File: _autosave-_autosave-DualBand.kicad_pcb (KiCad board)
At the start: 2 copper layers, 99.6 x 50.2 mm, 66 parts, among them J1 Conn_01x03_Male, J2 Conn_01x03_Male, J3 Conn_01x10_Male, J4 Conn_01x03_Male, J5 Conn_01x02_Male, J6 Conn_01x10_Male, J7 Conn_01x01_Male, P1 AD8402ARUZ1, SW1 SW_Push, U1 LD1117V33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

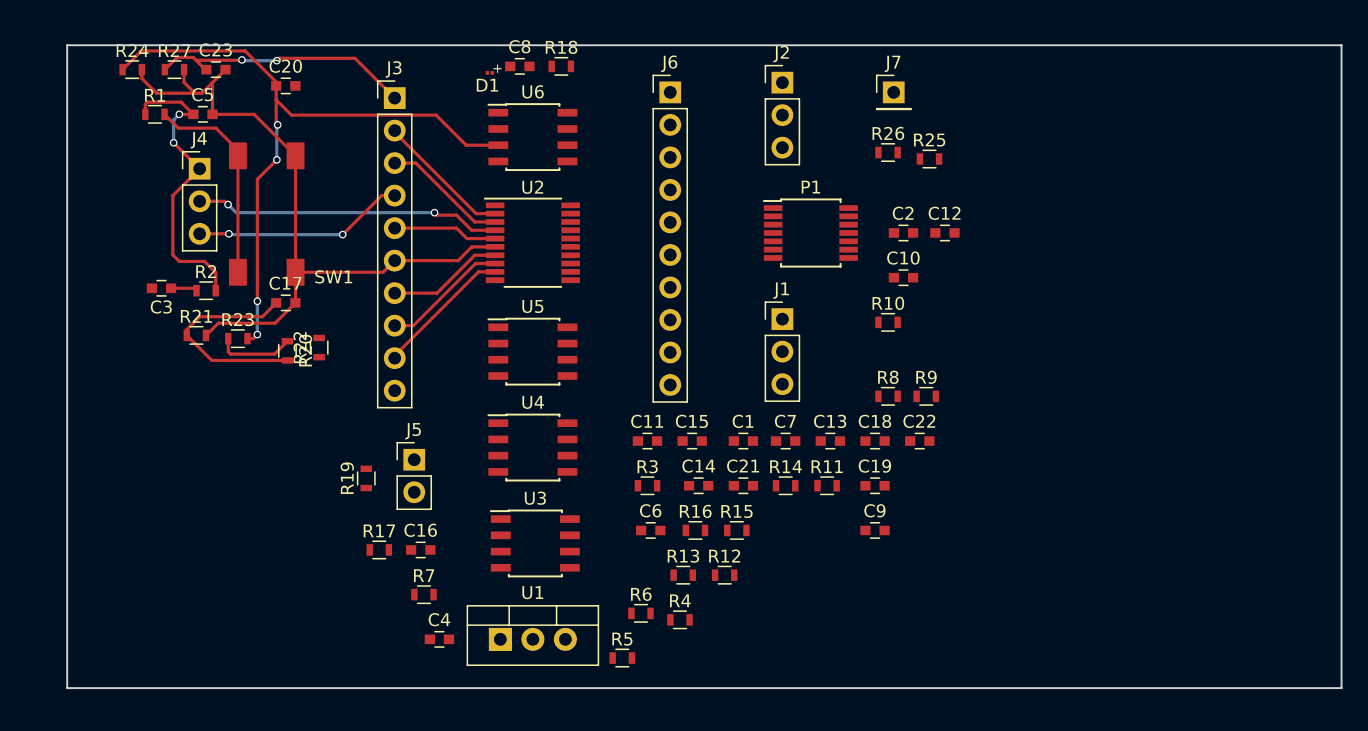
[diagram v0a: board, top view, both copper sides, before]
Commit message: Recreates PCB based on new layout
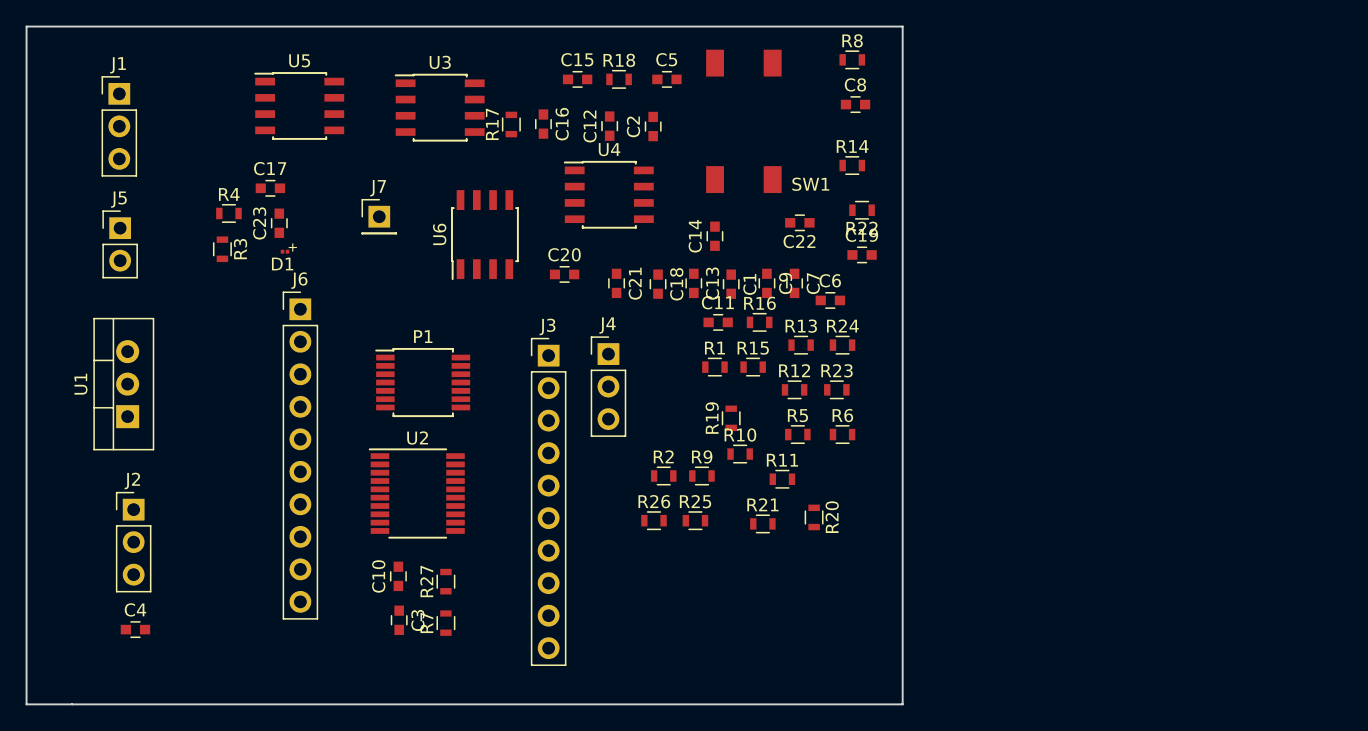
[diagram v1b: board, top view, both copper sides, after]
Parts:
- moved J2 60.7 mm to (117.6, 129.4)
- moved R24 59.5 mm to (173.0, 116.5)
- moved J1 54.7 mm to (116.5, 96.9)
- moved R1 48.0 mm to (163.0, 118.2)
- moved R4 47.4 mm to (125.0, 106.2)
- moved R23 47.0 mm to (172.5, 120.0)
- moved R21 46.6 mm to (166.8, 130.5)
- moved C10 45.8 mm to (138.3, 134.6), turned to 90 degrees
- moved R27 45.3 mm to (142.0, 135.0), turned to 90 degrees
- moved R22 43.8 mm to (174.5, 106.0), turned to 180 degrees
- moved R20 43.2 mm to (170.8, 130.0)
- moved J7 41.4 mm to (136.8, 106.5)
- moved R2 38.6 mm to (159.0, 126.7)
- moved R3 38.0 mm to (124.5, 109.0), turned to 270 degrees
- moved SW1 38.0 mm to (167.5, 94.5)
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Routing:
- net GND: track 57.1 -> 0.00 mm
- net Net-(C20-Pad1): track 53.8 -> 0.00 mm, vias 4 -> 0
- net Net-(C5-Pad1): track 24.3 -> 0.00 mm, vias 2 -> 0
- net Net-(J4-Pad2): track 24.0 -> 0.00 mm, vias 2 -> 0
- net Net-(C23-Pad1): track 21.0 -> 0.00 mm, vias 2 -> 0
- net Net-(C17-Pad1): track 17.0 -> 0.00 mm
- net Net-(J3-Pad4): track 16.5 -> 0.00 mm, vias 2 -> 0
- net Net-(R1-Pad2): track 16.4 -> 0.00 mm
- net Net-(J3-Pad9): track 10.7 -> 0.00 mm
- net Net-(J3-Pad2): track 10.6 -> 0.00 mm
- net /DVCC: track 10.3 -> 0.00 mm
- net Net-(J3-Pad8): track 9.85 -> 0.00 mm
- net Net-(J3-Pad3): track 9.75 -> 0.00 mm
- net Net-(J3-Pad7): track 9.07 -> 0.00 mm
- net +9V: track 6.14 -> 0.00 mm
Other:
- board size 99.6 x 50.2 mm -> 68.5 x 53 mm
